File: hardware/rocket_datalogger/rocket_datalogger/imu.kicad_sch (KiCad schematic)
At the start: 7 parts, among them U7 ICM-20948

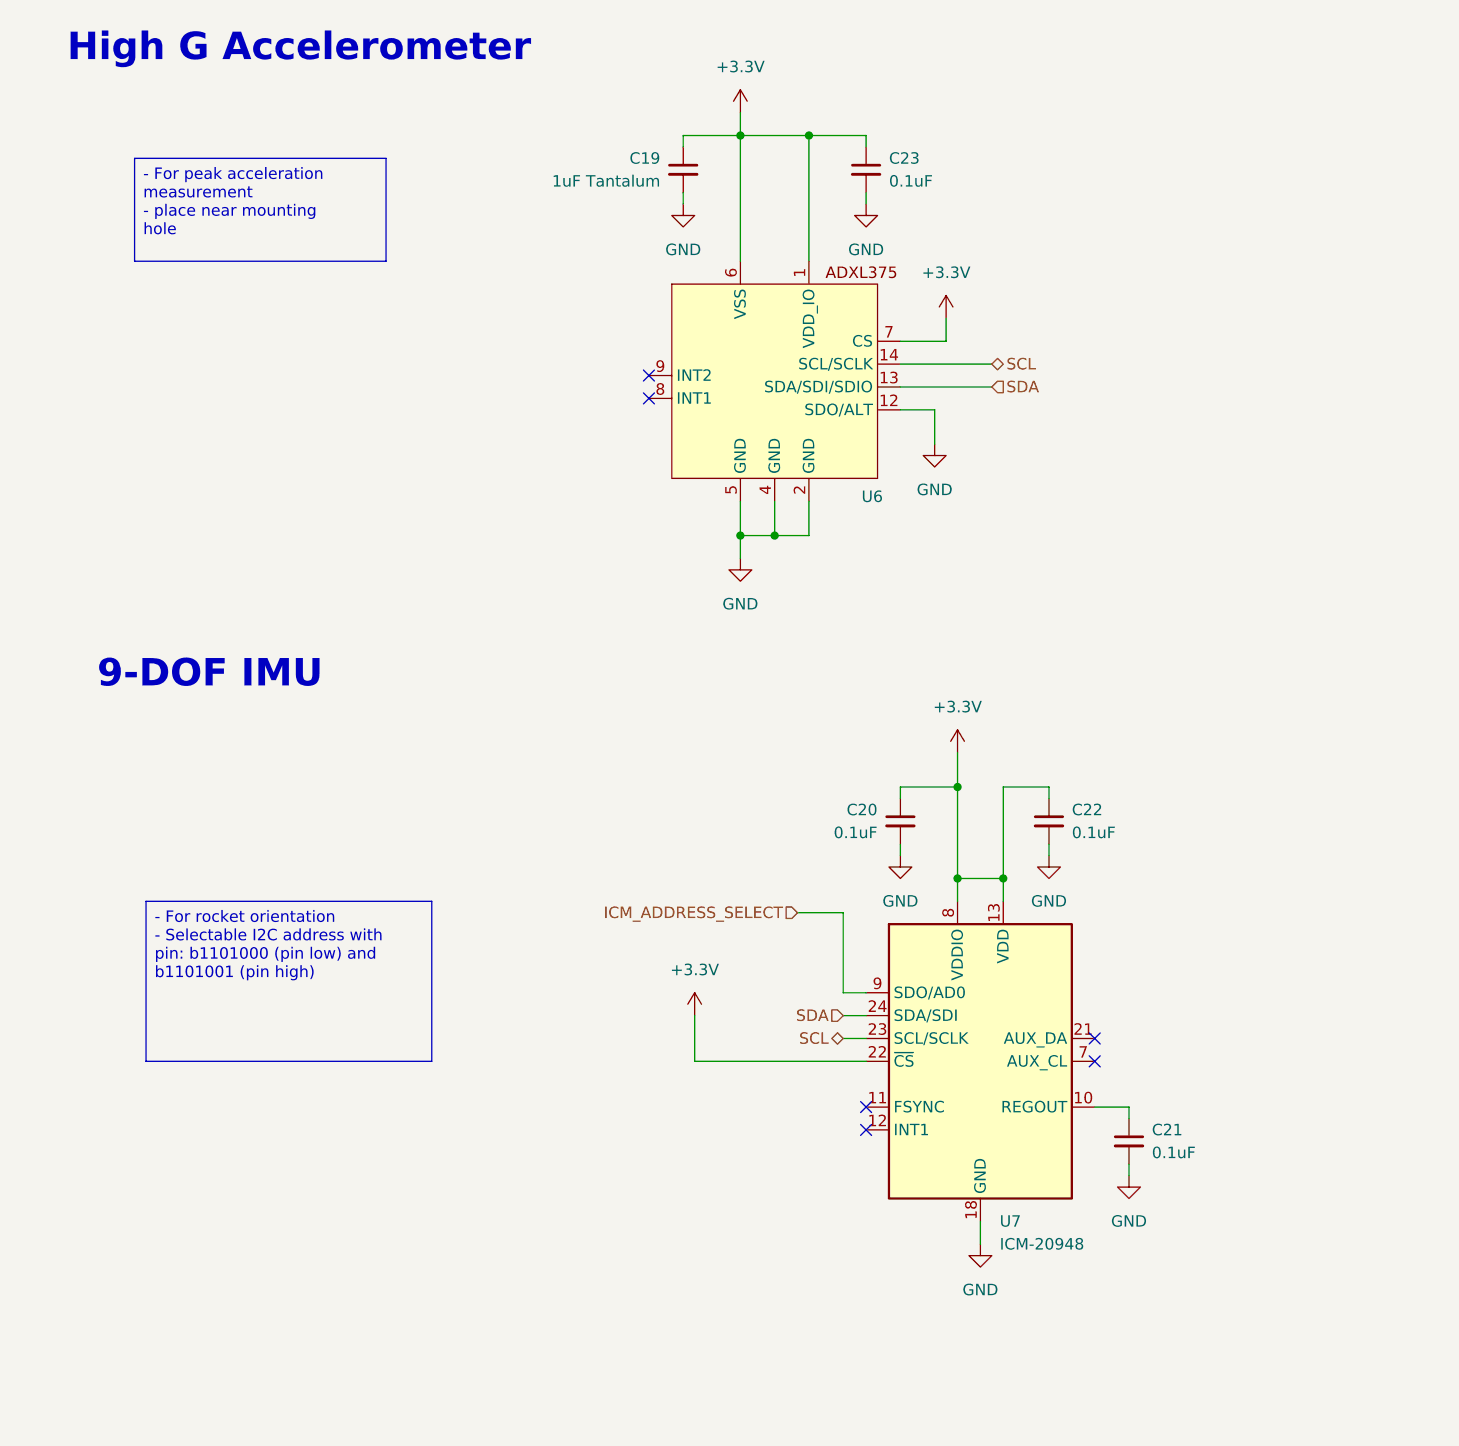
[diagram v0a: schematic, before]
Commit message: Changed IMU to BNO055
Previous IMU required 1.85V rail
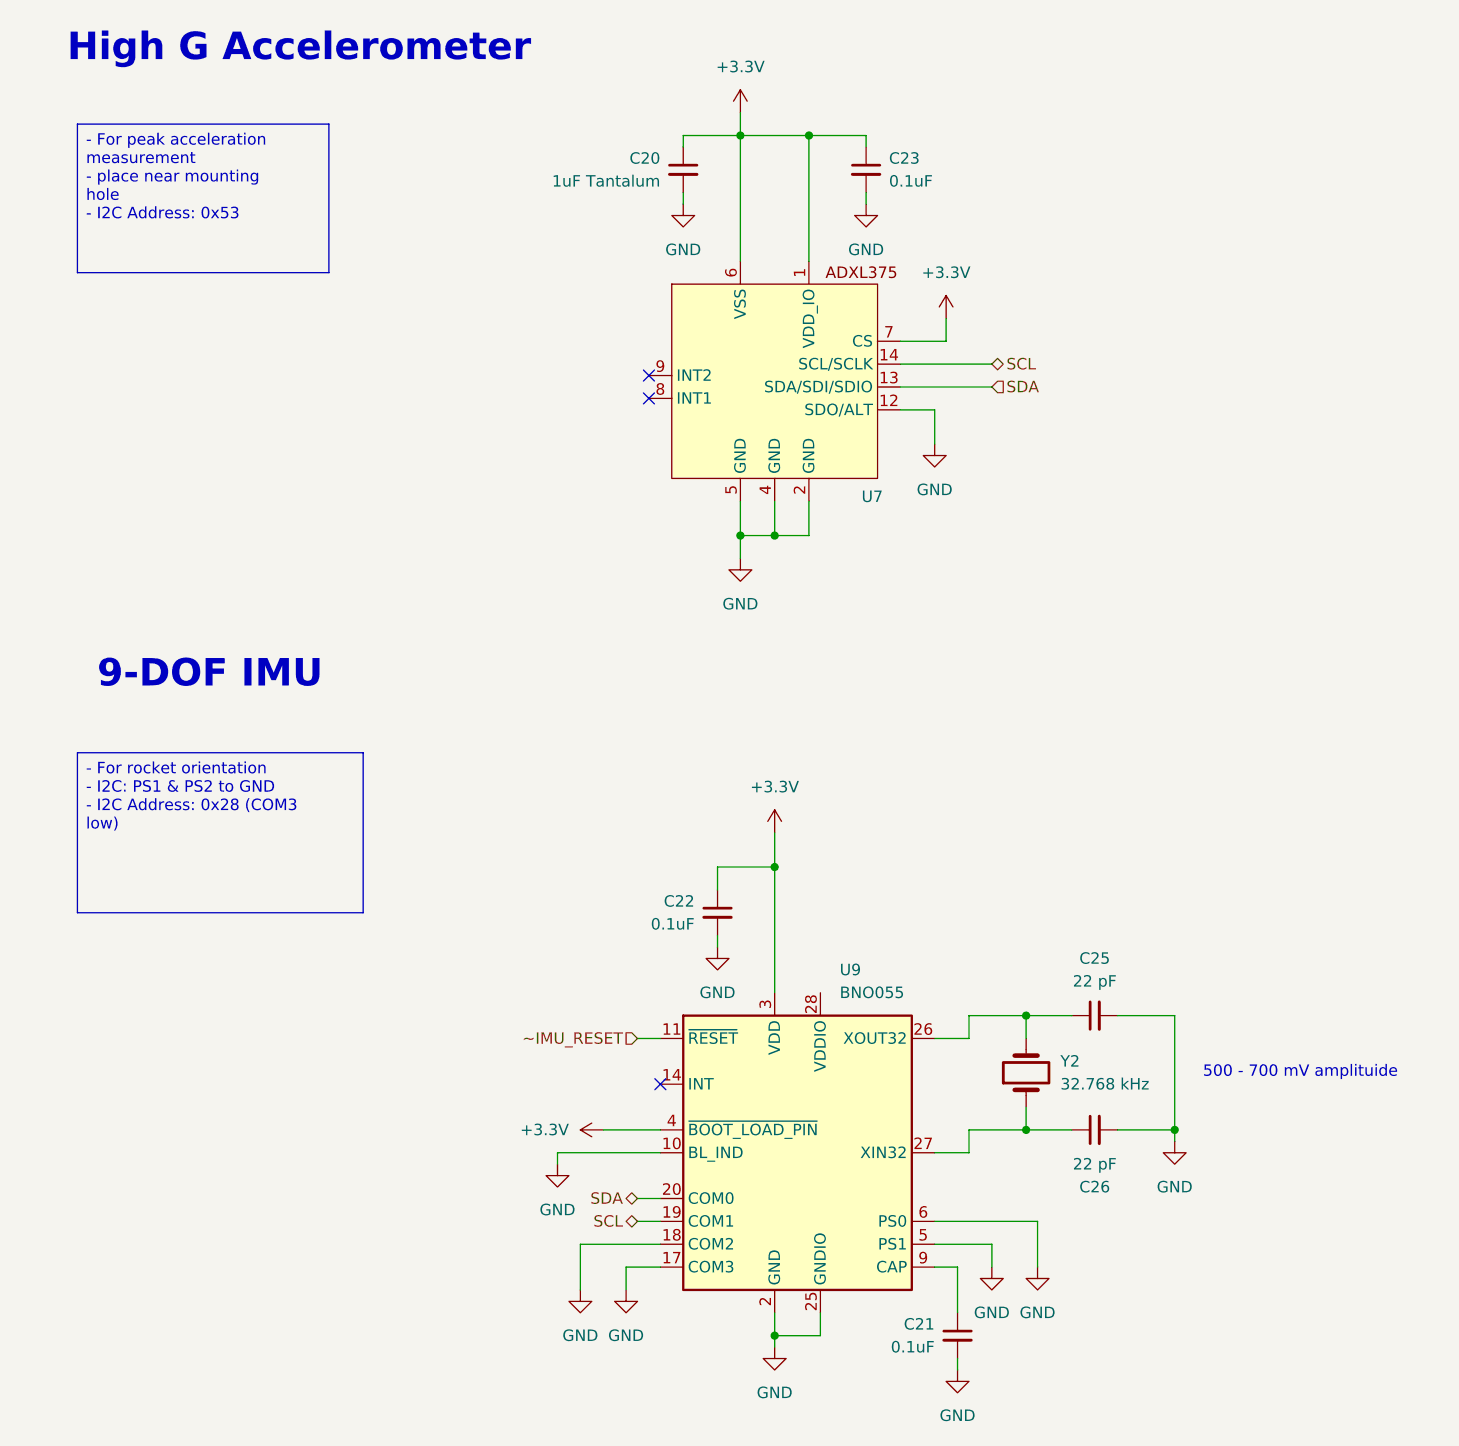
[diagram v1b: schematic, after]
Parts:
- removed C20: 0.1uF, symbol Device:C_Small
- removed U7: ICM-20948, Sensor_Motion:InvenSense_QFN-24_3x3mm_P0.4mm, symbol Sensor_Motion:ICM-20948
- added C25, C26: 22 pF, symbol Device:C_Small
- added U9: BNO055, Package_LGA:LGA-28_5.2x3.8mm_P0.5mm, symbol Sensor_Motion:BNO055
- added Y2: 32.768 kHz, symbol Device:Crystal
- renumbered C19 to C20, U6 to U7
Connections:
- net +3.3V: now also U9.3 (VDD), U9.4 (~{BOOT_LOAD_PIN})
- net GND: now also C25.2, C26.2, U9.10 (BL_IND), U9.17 (COM3), U9.18 (COM2), U9.2 (GND), U9.25 (GNDIO), U9.5 (PS1), U9.6 (PS0)
- net SCL: now also U9.19 (COM1)
- net SDA: now also U9.20 (COM0)
- net at C21.1: now also U9.9 (CAP)
- new net: C26.1, U9.27 (XIN32), Y2.1
- new net: C25.1, U9.26 (XOUT32), Y2.2
- new net ~IMU_RESET: U9.11 (~{RESET})
- no-connect marks 6 -> 3
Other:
- note added: "500 - 700 mV amplituide"

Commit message: fixed minor hardware issues
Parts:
- added R14: 10k, Resistor_SMD:R_0603_1608Metric, symbol Device:R_Small
- C20: footprint (none) -> Capacitor_SMD:C_0603_1608Metric
- C21: renamed from C22; footprint (none) -> Capacitor_SMD:C_0603_1608Metric
- C22: renamed from C23; footprint (none) -> Capacitor_SMD:C_0603_1608Metric
- C23: renamed from C21; footprint (none) -> Capacitor_SMD:C_0603_1608Metric
- C24: renamed from C25; footprint (none) -> Capacitor_SMD:C_0603_1608Metric
- C25: renamed from C26; footprint (none) -> Capacitor_SMD:C_0603_1608Metric
- renumbered U9 to U8
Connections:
- net +3.3V: now also U8.28 (VDDIO), R14.1; no longer U8.4 (~{BOOT_LOAD_PIN})
- net IMU_INT: now reaches U8.14 (INT)
- new net: R14.2, U8.4 (~{BOOT_LOAD_PIN})
- no-connect marks 3 -> 2

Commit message: Minor revision
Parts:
- U7: footprint (none) -> Package_LGA:LGA-14_3x5mm_P0.8mm_LayoutBorder1x6y
- Y2: value 32.768 kHz -> ECX-.327-CDX-1293; footprint (none) -> Crystal:Crystal_SMD_3215-2Pin_3.2x1.5mm
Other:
- note added: "32.768 kHz, 12.5 pF, 70 kOhm"
- note removed: "500 - 700 mV amplituide"
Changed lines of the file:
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@@
 		)
 	)
-	(text "500 - 700 mV amplituide"
-		(exclude_from_sim no)
-		(at 152.4 132.08 0)
+	(text "32.768 kHz, 12.5 pF, 70 kOhm"
+		(exclude_from_sim no)
+		(at 150.368 130.302 0)
 		(effects
 			(font
@@
 	)
 	(junction
+		(at 147.32 138.43)
+		(diameter 0)
+		(color 0 0 0 0)
+	)
+	(junction
 		(at 90.17 27.94)
 		(diameter 0)
@@
 	)
 	(junction
-		(at 138.43 138.43)
-		(diameter 0)
-		(color 0 0 0 0)
-	)
-	(junction
 		(at 90.17 72.39)
 		(diameter 0)
@@
 	(wire
 		(pts
-			(xy 138.43 125.73) (xy 138.43 138.43)
+			(xy 147.32 125.73) (xy 147.32 138.43)
 		)
 		(stroke
@@
 	(wire
 		(pts
-			(xy 132.08 125.73) (xy 138.43 125.73)
+			(xy 132.08 125.73) (xy 147.32 125.73)
 		)
 		(stroke
@@
 	(wire
 		(pts
-			(xy 138.43 138.43) (xy 132.08 138.43)
+			(xy 132.08 138.43) (xy 147.32 138.43)
 		)
 		(stroke
@@
 	(wire
 		(pts
-			(xy 138.43 139.7) (xy 138.43 138.43)
+			(xy 147.32 139.7) (xy 147.32 138.43)
 		)
 		(stroke
@@
 			)
 		)
-		(property "Value" "32.768 kHz"
+		(property "Value" "ECX-.327-CDX-1293"
 			(at 125.73 133.3499 90)
 			(effects
@@
 			)
 		)
-		(property "Footprint" ""
+		(property "Footprint" "Crystal:Crystal_SMD_3215-2Pin_3.2x1.5mm"
 			(at 121.92 132.08 0)
 			(effects
@@
 	(symbol
 		(lib_id "power:GND")
-		(at 138.43 139.7 0)
+		(at 147.32 139.7 0)
 		(unit 1)
 		(exclude_from_sim no)
@@
 		(fields_autoplaced yes)
 		(property "Reference" "#PWR070"
-			(at 138.43 146.05 0)
+			(at 147.32 146.05 0)
 			(effects
 				(font
@@
 		)
 		(property "Value" "GND"
-			(at 138.43 144.78 0)
+			(at 147.32 144.78 0)
 			(effects
 				(font
@@
 		)
 		(property "Footprint" ""
-			(at 138.43 139.7 0)
+			(at 147.32 139.7 0)
 			(effects
 				(font
@@
 		)
 		(property "Datasheet" ""
-			(at 138.43 139.7 0)
+			(at 147.32 139.7 0)
 			(effects
 				(font
@@
 		)
 		(property "Description" "Power symbol creates a global label with name \"GND\" , ground"
-			(at 138.43 139.7 0)
+			(at 147.32 139.7 0)
 			(effects
 				(font
@@
 			)
 		)
-		(property "Footprint" ""
+		(property "Footprint" "Package_LGA:LGA-14_3x5mm_P0.8mm_LayoutBorder1x6y"
 			(at 93.98 55.88 0)
 			(effects
